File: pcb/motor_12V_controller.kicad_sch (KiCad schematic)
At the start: 39 parts, among them IC1 RP2040-ZERO, J1 01x02, J2 01x02, U1 AP63200WU, U2 L293D

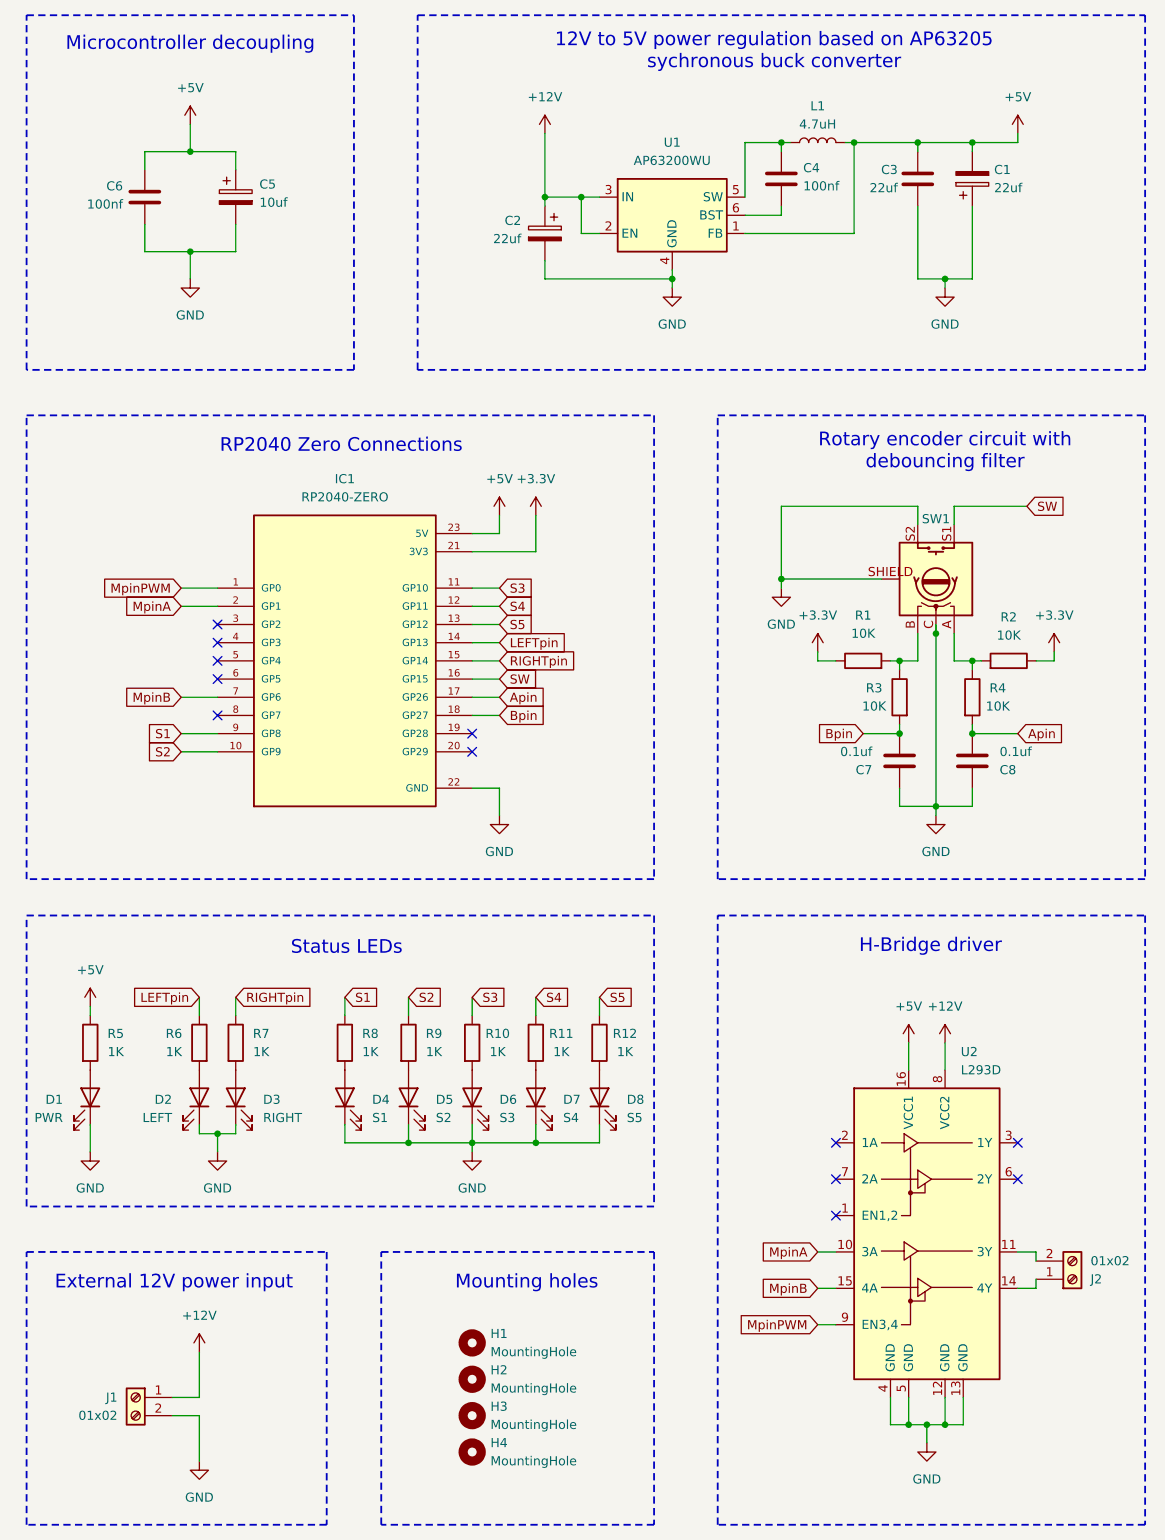
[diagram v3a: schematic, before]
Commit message: Fixed the H-Bridge decoupling. Added additional capasitor for +12V power input.
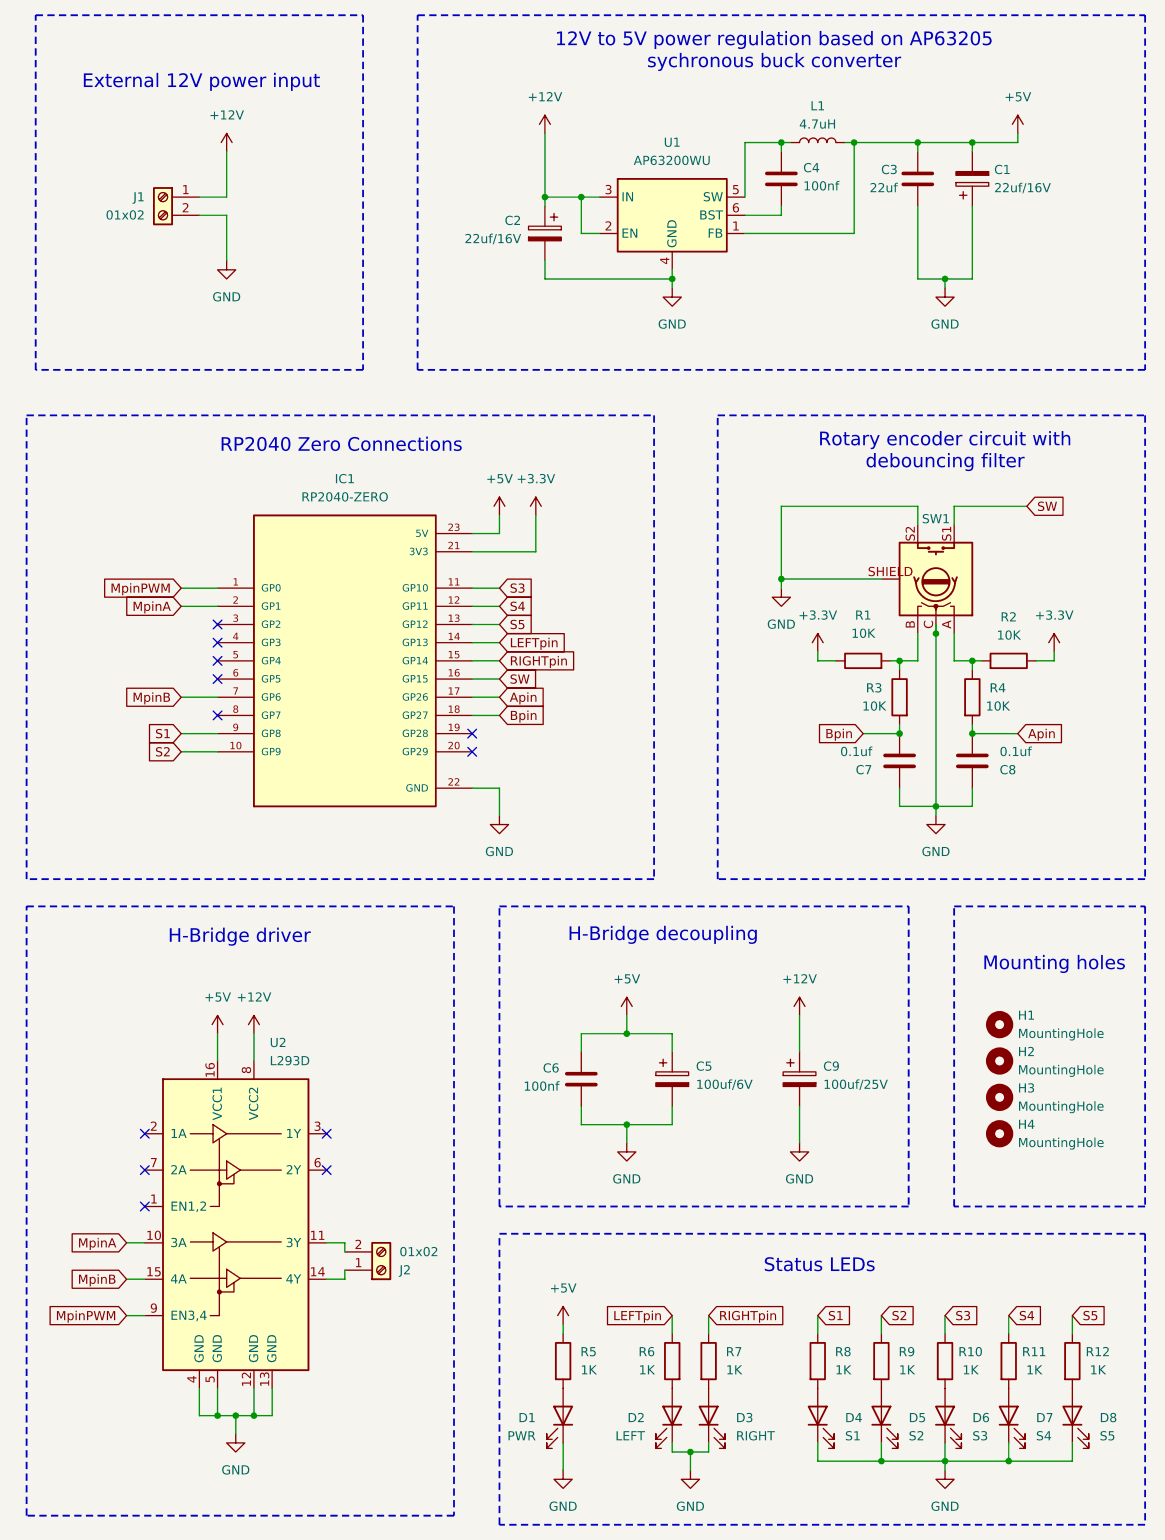
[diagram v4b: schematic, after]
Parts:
- added C9: 100uf/25V, Capacitor_THT:CP_Radial_D4.0mm_P1.50mm, symbol Device:C_Polarized
- C1, C2: value 22uf -> 22uf/16V
- C5: value 10uf -> 100uf/6V
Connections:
- net +12V: now also C9.1
- net GND: now also C9.2
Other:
- note added: "H-Bridge decoupling"
- note removed: "Microcontroller decoupling"
- moved on the sheet: C5, C6, D1, D2, D3, D4, D5, D6, D7, D8, H1, H2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
